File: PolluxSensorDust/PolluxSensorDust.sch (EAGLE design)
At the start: 0 parts

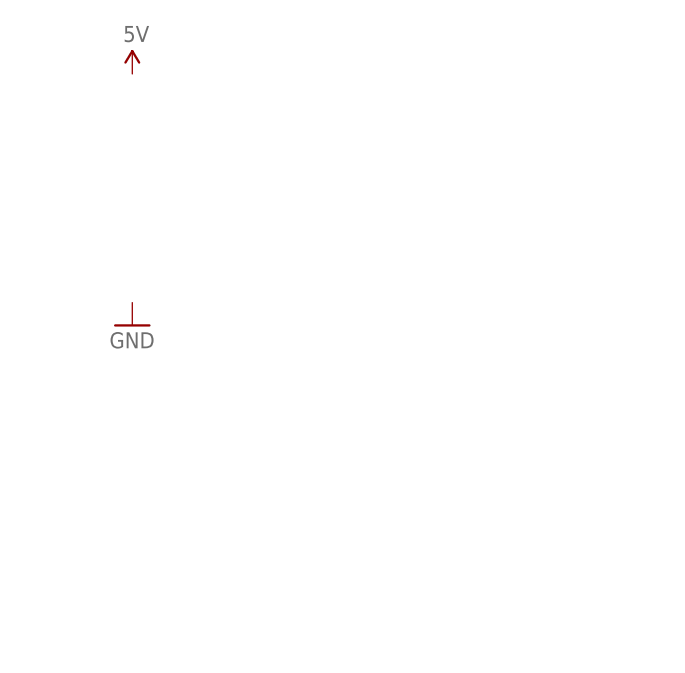
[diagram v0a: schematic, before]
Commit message: add dust sensor schematics and board
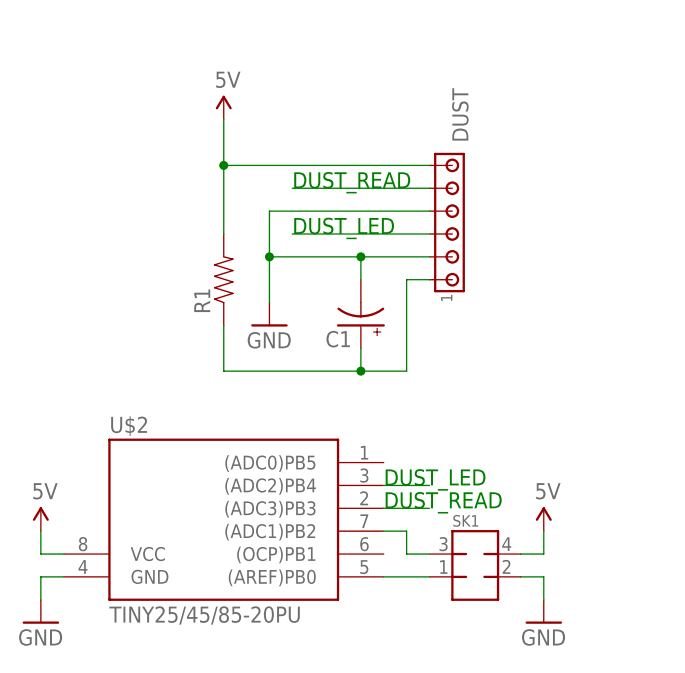
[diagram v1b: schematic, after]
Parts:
- added C1: (no value), SparkFun:CAP_POLPTH4
- added DUST: (no value), con-amp:MTA06-100
- added R1: (no value), SparkFun:RESISTORAXIAL-0.3
- added SK1: (no value), jt-con-micromatch:MMATCH-8-PTH
- added U$2: TINY25/45/85-20PU, avr-7:TINY25/45/85-20PU
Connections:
- new net 5V: DUST.6, R1.2, SK1.4, U$2.VCC
- new net DUST_LED: DUST.3, U$2.(ADC2)PB4
- new net DUST_READ: DUST.5, U$2.(ADC3)PB3
- new net GND: C1.-, DUST.2, DUST.4, SK1.2, U$2.GND
- new net N$1: SK1.3, U$2.(ADC1)PB2
- new net N$2: SK1.1, U$2.(AREF)PB0
- new net N$4: C1.+, DUST.1, R1.1
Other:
- note added: "DUST_LED"
- note added: "DUST_READ"
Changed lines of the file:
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@@
 <part name="U$1" library="SparkFun" deviceset="5V" device=""/>
 <part name="GND1" library="SparkFun" deviceset="GND" device=""/>
+<part name="SK1" library="jt-con-micromatch" deviceset="MMATCH-8-*" device="PTH"/>
+<part name="U$2" library="avr-7" deviceset="TINY25/45/85" device="-20PU"/>
+<part name="C1" library="SparkFun" deviceset="CAP_POL" device="PTH4"/>
+<part name="R1" library="SparkFun" deviceset="RESISTOR" device="AXIAL-0.3"/>
+<part name="DUST" library="con-amp" deviceset="MTA06-100" device=""/>
+<part name="U$3" library="SparkFun" deviceset="5V" device=""/>
+<part name="U$4" library="SparkFun" deviceset="5V" device=""/>
+<part name="GND2" library="SparkFun" deviceset="GND" device=""/>
+<part name="GND3" library="SparkFun" deviceset="GND" device=""/>
 </parts>
 <sheets>
 <sheet>
 <plain>
+<text x="71.12" y="30.48" size="1.778" layer="91">DUST_READ</text>
+<text x="71.12" y="33.02" size="1.778" layer="91">DUST_LED</text>
+<text x="60.96" y="60.96" size="1.778" layer="91">DUST_LED</text>
+<text x="60.96" y="66.04" size="1.778" layer="91">DUST_READ</text>
 </plain>
 <instances>
-<instance part="U$1" gate="G$1" x="43.18" y="78.74"/>
-<instance part="GND1" gate="1" x="43.18" y="50.8"/>
+<instance part="U$1" gate="G$1" x="53.34" y="73.66"/>
+<instance part="GND1" gate="1" x="88.9" y="17.78"/>
+<instance part="SK1" gate="G$1" x="81.28" y="22.86"/>
+<instance part="U$2" gate="G$1" x="53.34" y="27.94"/>
+<instance part="C1" gate="G$1" x="68.58" y="50.8" rot="R180"/>
+<instance part="R1" gate="G$1" x="53.34" y="55.88" rot="R90"/>
+<instance part="DUST" gate="G$1" x="78.74" y="60.96" rot="MR90"/>
+<instance part="U$3" gate="G$1" x="33.02" y="27.94"/>
+<instance part="U$4" gate="G$1" x="88.9" y="27.94"/>
+<instance part="GND2" gate="1" x="33.02" y="17.78"/>
+<instance part="GND3" gate="1" x="58.42" y="50.8"/>
 </instances>
 <busses>
 </busses>
 <nets>
+<net name="N$2" class="0">
+<segment>
+<pinref part="SK1" gate="G$1" pin="1"/>
+<pinref part="U$2" gate="G$1" pin="(AREF)PB0"/>
+<wire x1="76.2" y1="22.86" x2="71.12" y2="22.86" width="0.1524" layer="91"/>
+</segment>
+</net>
+<net name="5V" class="0">
+<segment>
+<pinref part="SK1" gate="G$1" pin="4"/>
+<wire x1="86.36" y1="25.4" x2="88.9" y2="25.4" width="0.1524" layer="91"/>
+<pinref part="U$4" gate="G$1" pin="5V"/>
+<wire x1="88.9" y1="25.4" x2="88.9" y2="27.94" width="0.1524" layer="91"/>
+</segment>
+<segment>
+<pinref part="U$2" gate="G$1" pin="VCC"/>
+<wire x1="35.56" y1="25.4" x2="33.02" y2="25.4" width="0.1524" layer="91"/>
+<pinref part="U$3" gate="G$1" pin="5V"/>
+<wire x1="33.02" y1="25.4" x2="33.02" y2="27.94" width="0.1524" layer="91"/>
+</segment>
+<segment>
+<pinref part="R1" gate="G$1" pin="2"/>
+<pinref part="U$1" gate="G$1" pin="5V"/>
+<wire x1="53.34" y1="60.96" x2="53.34" y2="68.58" width="0.1524" layer="91"/>
+<wire x1="53.34" y1="68.58" x2="53.34" y2="73.66" width="0.1524" layer="91"/>
+<wire x1="53.34" y1="68.58" x2="76.2" y2="68.58" width="0.1524" layer="91"/>
+<pinref part="DUST" gate="G$1" pin="6"/>
+<junction x="53.34" y="68.58"/>
+</segment>
+</net>
+<net name="DUST_LED" class="0">
+<segment>
+<pinref part="DUST" gate="G$1" pin="3"/>
+<wire x1="76.2" y1="60.96" x2="60.96" y2="60.96" width="0.1524" layer="91"/>
+</segment>
+<segment>
+<pinref part="U$2" gate="G$1" pin="(ADC2)PB4"/>
+<wire x1="71.12" y1="33.02" x2="76.2" y2="33.02" width="0.1524" layer="91"/>
+</segment>
+</net>
+<net name="GND" class="0">
+<segment>
+<pinref part="U$2" gate="G$1" pin="GND"/>
+<wire x1="35.56" y1="22.86" x2="33.02" y2="22.86" width="0.1524" layer="91"/>
+<pinref part="GND2" gate="1" pin="GND"/>
+<wire x1="33.02" y1="22.86" x2="33.02" y2="20.32" width="0.1524" layer="91"/>
+</segment>
+<segment>
+<pinref part="SK1" gate="G$1" pin="2"/>
+<wire x1="86.36" y1="22.86" x2="88.9" y2="22.86" width="0.1524" layer="91"/>
+<pinref part="GND1" gate="1" pin="GND"/>
+<wire x1="88.9" y1="22.86" x2="88.9" y2="20.32" width="0.1524" layer="91"/>
+</segment>
+<segment>
+<pinref part="GND3" gate="1" pin="GND"/>
+<wire x1="58.42" y1="53.34" x2="58.42" y2="58.42" width="0.1524" layer="91"/>
+<pinref part="DUST" gate="G$1" pin="2"/>
+<wire x1="76.2" y1="58.42" x2="68.58" y2="58.42" width="0.1524" layer="91"/>
+<pinref part="C1" gate="G$1" pin="-"/>
+<wire x1="68.58" y1="58.42" x2="68.58" y2="55.88" width="0.1524" layer="91"/>
+<wire x1="58.42" y1="58.42" x2="68.58" y2="58.42" width="0.1524" layer="91"/>
+<wire x1="58.42" y1="58.42" x2="58.42" y2="63.5" width="0.1524" layer="91"/>
+<pinref part="DUST" gate="G$1" pin="4"/>
+<wire x1="58.42" y1="63.5" x2="76.2" y2="63.5" width="0.1524" layer="91"/>
+<junction x="58.42" y="58.42"/>
+<junction x="68.58" y="58.42"/>
+</segment>
+</net>
+<net name="N$1" class="0">
+<segment>
+<pinref part="U$2" gate="G$1" pin="(ADC1)PB2"/>
+<wire x1="71.12" y1="27.94" x2="73.66" y2="27.94" width="0.1524" layer="91"/>
+<wire x1="73.66" y1="27.94" x2="73.66" y2="25.4" width="0.1524" layer="91"/>
+<pinref part="SK1" gate="G$1" pin="3"/>
+<wire x1="73.66" y1="25.4" x2="76.2" y2="25.4" width="0.1524" layer="91"/>
+</segment>
+</net>
+<net name="DUST_READ" class="0">
+<segment>
+<pinref part="DUST" gate="G$1" pin="5"/>
+<wire x1="76.2" y1="66.04" x2="60.96" y2="66.04" width="0.1524" layer="91"/>
+</segment>
+<segment>
+<pinref part="U$2" gate="G$1" pin="(ADC3)PB3"/>
+<wire x1="71.12" y1="30.48" x2="76.2" y2="30.48" width="0.1524" layer="91"/>
+</segment>
+</net>
+<net name="N$4" class="0">
+<segment>
+<pinref part="R1" gate="G$1" pin="1"/>
+<wire x1="53.34" y1="50.8" x2="53.34" y2="45.72" width="0.1524" layer="91"/>
+<pinref part="DUST" gate="G$1" pin="1"/>
+<wire x1="76.2" y1="55.88" x2="73.66" y2="55.88" width="0.1524" layer="91"/>
+<wire x1="73.66" y1="55.88" x2="73.66" y2="45.72" width="0.1524" layer="91"/>
+<wire x1="73.66" y1="45.72" x2="68.58" y2="45.72" width="0.1524" layer="91"/>
+<pinref part="C1" gate="G$1" pin="+"/>
+<wire x1="68.58" y1="45.72" x2="53.34" y2="45.72" width="0.1524" layer="91"/>
+<wire x1="68.58" y1="48.26" x2="68.58" y2="45.72" width="0.1524" layer="91"/>
+<junction x="68.58" y="45.72"/>
+</segment>
+</net>
 </nets>
 </sheet>

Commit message: improve sensor board
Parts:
- C1: value (none) -> 220 uF
- R1: value (none) -> 150
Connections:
- removed net N$2: SK1.1, U$2.(AREF)PB0
- new net SDA: SK1.4, U$2.(AREF)PB0
- net 5V: now also SK1.1; no longer SK1.4
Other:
- note added: "SCL"
- note added: "SDA"
- moved on the sheet: SK1
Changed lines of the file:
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@@
 <part name="SK1" library="jt-con-micromatch" deviceset="MMATCH-8-*" device="PTH"/>
 <part name="U$2" library="avr-7" deviceset="TINY25/45/85" device="-20PU"/>
-<part name="C1" library="SparkFun" deviceset="CAP_POL" device="PTH4"/>
-<part name="R1" library="SparkFun" deviceset="RESISTOR" device="AXIAL-0.3"/>
+<part name="C1" library="SparkFun" deviceset="CAP_POL" device="PTH4" value="220 uF"/>
+<part name="R1" library="SparkFun" deviceset="RESISTOR" device="AXIAL-0.3" value="150"/>
 <part name="DUST" library="con-amp" deviceset="MTA06-100" device=""/>
 <part name="U$3" library="SparkFun" deviceset="5V" device=""/>
@@
 <text x="60.96" y="60.96" size="1.778" layer="91">DUST_LED</text>
 <text x="60.96" y="66.04" size="1.778" layer="91">DUST_READ</text>
+<text x="71.12" y="27.94" size="1.778" layer="91">SCL</text>
+<text x="71.12" y="22.86" size="1.778" layer="91">SDA</text>
+<text x="96.52" y="27.94" size="1.778" layer="91">SDA</text>
 </plain>
 <instances>
 <instance part="U$1" gate="G$1" x="53.34" y="73.66"/>
-<instance part="GND1" gate="1" x="88.9" y="17.78"/>
-<instance part="SK1" gate="G$1" x="81.28" y="22.86"/>
+<instance part="GND1" gate="1" x="99.06" y="20.32"/>
+<instance part="SK1" gate="G$1" x="91.44" y="25.4"/>
 <instance part="U$2" gate="G$1" x="53.34" y="27.94"/>
 <instance part="C1" gate="G$1" x="68.58" y="50.8" rot="R180"/>
@@
 <instance part="DUST" gate="G$1" x="78.74" y="60.96" rot="MR90"/>
 <instance part="U$3" gate="G$1" x="33.02" y="27.94"/>
-<instance part="U$4" gate="G$1" x="88.9" y="27.94"/>
+<instance part="U$4" gate="G$1" x="83.82" y="38.1"/>
 <instance part="GND2" gate="1" x="33.02" y="17.78"/>
 <instance part="GND3" gate="1" x="58.42" y="50.8"/>
@@
 </busses>
 <nets>
-<net name="N$2" class="0">
-<segment>
-<pinref part="SK1" gate="G$1" pin="1"/>
-<pinref part="U$2" gate="G$1" pin="(AREF)PB0"/>
-<wire x1="76.2" y1="22.86" x2="71.12" y2="22.86" width="0.1524" layer="91"/>
-</segment>
-</net>
 <net name="5V" class="0">
-<segment>
-<pinref part="SK1" gate="G$1" pin="4"/>
-<wire x1="86.36" y1="25.4" x2="88.9" y2="25.4" width="0.1524" layer="91"/>
-<pinref part="U$4" gate="G$1" pin="5V"/>
-<wire x1="88.9" y1="25.4" x2="88.9" y2="27.94" width="0.1524" layer="91"/>
-</segment>
 <segment>
 <pinref part="U$2" gate="G$1" pin="VCC"/>
@@
 <pinref part="DUST" gate="G$1" pin="6"/>
 <junction x="53.34" y="68.58"/>
+</segment>
+<segment>
+<pinref part="SK1" gate="G$1" pin="1"/>
+<wire x1="86.36" y1="25.4" x2="83.82" y2="25.4" width="0.1524" layer="91"/>
+<wire x1="83.82" y1="25.4" x2="83.82" y2="38.1" width="0.1524" layer="91"/>
+<pinref part="U$4" gate="G$1" pin="5V"/>
 </segment>
 </net>
@@
 </segment>
 <segment>
-<pinref part="SK1" gate="G$1" pin="2"/>
-<wire x1="86.36" y1="22.86" x2="88.9" y2="22.86" width="0.1524" layer="91"/>
-<pinref part="GND1" gate="1" pin="GND"/>
-<wire x1="88.9" y1="22.86" x2="88.9" y2="20.32" width="0.1524" layer="91"/>
-</segment>
-<segment>
 <pinref part="GND3" gate="1" pin="GND"/>
 <wire x1="58.42" y1="53.34" x2="58.42" y2="58.42" width="0.1524" layer="91"/>
@@
 <junction x="68.58" y="58.42"/>
 </segment>
-</net>
-<net name="N$1" class="0">
 <segment>
-<pinref part="U$2" gate="G$1" pin="(ADC1)PB2"/>
-<wire x1="71.12" y1="27.94" x2="73.66" y2="27.94" width="0.1524" layer="91"/>
-<wire x1="73.66" y1="27.94" x2="73.66" y2="25.4" width="0.1524" layer="91"/>
-<pinref part="SK1" gate="G$1" pin="3"/>
-<wire x1="73.66" y1="25.4" x2="76.2" y2="25.4" width="0.1524" layer="91"/>
+<pinref part="SK1" gate="G$1" pin="2"/>
+<pinref part="GND1" gate="1" pin="GND"/>
+<wire x1="96.52" y1="25.4" x2="99.06" y2="25.4" width="0.1524" layer="91"/>
+<wire x1="99.06" y1="25.4" x2="99.06" y2="22.86" width="0.1524" layer="91"/>
 </segment>
 </net>
@@
 </segment>
 </net>
+<net name="N$1" class="0">
+<segment>
+<pinref part="U$2" gate="G$1" pin="(ADC1)PB2"/>
+<pinref part="SK1" gate="G$1" pin="3"/>
+<wire x1="71.12" y1="27.94" x2="86.36" y2="27.94" width="0.1524" layer="91"/>
+</segment>
+</net>
+<net name="SDA" class="0">
+<segment>
+<pinref part="U$2" gate="G$1" pin="(AREF)PB0"/>
+<wire x1="71.12" y1="22.86" x2="76.2" y2="22.86" width="0.1524" layer="91"/>
+</segment>
+<segment>
+<pinref part="SK1" gate="G$1" pin="4"/>
+<wire x1="96.52" y1="27.94" x2="101.6" y2="27.94" width="0.1524" layer="91"/>
+</segment>
+</net>
